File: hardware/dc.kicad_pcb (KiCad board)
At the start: 4 copper layers, 80 x 80 mm, 70 parts, among them P1 CON-SENSOR2, P2 DEBUG, P3 BOOT, P4 OUT, P5 GPIO, P6 IN, Q1 PSMN5R6-60YLX, U1 XMC1???, U2 DRILL, U3 DRILL, U4 DRILL, U5 DRILL, U6 VNH5019A-E, U7 LTV-827

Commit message: new DRV8701 design
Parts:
- C1: footprint C0402E -> kicad-libraries:C0402E
- C4: footprint C0603F -> kicad-libraries:C0603F
- D1, D10, D11, D12, D8, D9: footprint D0603F -> kicad-libraries:D0603F
- P2: footprint DEBUG_PAD -> kicad-libraries:DEBUG_PAD
- P3: footprint SolderJumper -> kicad-libraries:SolderJumper
- P6: footprint kicad-libraries:OQ_2P_5mm_Vertical -> kicad-libraries:OQ_2P_5mm_Vertical_Black
- RP1: footprint 4X0603 -> kicad-libraries:4X0603
- U1: footprint QFN24-4x4mm-0.5mm -> kicad-libraries:QFN24-4x4mm-0.5mm
- U2, U3, U4, U5: footprint DRILL_NP -> kicad-libraries:DRILL_NP

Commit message: new design
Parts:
- removed the Fiducial_Mark at (93.5, 120.5)
- removed the Fiducial_Mark at (88.5, 168.5)
- removed the Fiducial_Mark at (134.5, 118.5)
- removed the G*** at (99.5, 163.5)
- removed PTC1: VC080526C580DP, kicad-libraries:R0805E
- removed RP2: 3,3k, kicad-libraries:4X0603
- removed RP3: 1k, kicad-libraries:0603X4
- removed VAL: CE_5mm, kicad-libraries:CE_5mm
- removed VAL: WEEE_7mm, kicad-libraries:WEEE_7mm
- added C17: DNP, kicad-libraries:C0603F, F.Cu at (124.3, 149.1)
- added C18: 1uF/100V, kicad-libraries:C1206E, F.Cu at (66.0, 131.6)
- added C19: 220uF/100V/UVY2A221MHD1TO, kicad-libraries:ELKO_RAD_12, F.Cu at (66.8, 142.2)
- added C20: DNP, kicad-libraries:C0603F, F.Cu at (94.2, 152.8)
- added C21: DNP, kicad-libraries:C0603F, F.Cu at (111.3, 149.1)
- added C22: 220uF/100V/UVY2A221MHD1TO, kicad-libraries:ELKO_RAD_12, F.Cu at (66.8, 156.0)
- added C23: 1nF/100V, kicad-libraries:C0603F, F.Cu at (122.5, 176.7)
- added C24: 1nF/100V, kicad-libraries:C0603F, F.Cu at (106.5, 176.7)
- added C25: 220uF/100V/UVY2A221MHD1TO, kicad-libraries:ELKO_RAD_12, F.Cu at (79.1, 149.1)
- added C26: 220uF/100V/UVY2A221MHD1TO, kicad-libraries:ELKO_RAD_12, F.Cu at (79.1, 135.1)
- added D13: SMBJ36CA, kicad-libraries:SMB, F.Cu at (74.5, 165.4)
- added Q2: CSD19533Q5A, kicad-libraries:SON_5x6mm, F.Cu at (121.0, 150.9)
- added Q3: CSD19533Q5A, kicad-libraries:SON_5x6mm, F.Cu at (97.5, 151.0)
- added Q4: CSD19533Q5A, kicad-libraries:SON_5x6mm, F.Cu at (108.0, 150.9)
- added Q5: CSD19533Q5A, kicad-libraries:SON_5x6mm, F.Cu at (78.4, 159.8)
- added R18: TBD, kicad-libraries:R0603F, F.Cu at (118.2, 118.8)
- added R19: TBD, kicad-libraries:R0603F, F.Cu at (119.5, 118.8)
- added R20: 0, kicad-libraries:R0603F, F.Cu at (100.8, 152.8)
- added R21: 0, kicad-libraries:R0603F, F.Cu at (104.7, 149.1)
- added R22: 0, kicad-libraries:R0603F, F.Cu at (134.8, 152.8)
- added R23: 0, kicad-libraries:R0603F, F.Cu at (117.7, 149.1)
- added R24: 0,01/WSHM2818R0100FEA, kicad-libraries:R2818, F.Cu at (114.5, 138.2)
- added R25: 100k, kicad-libraries:R0603F, F.Cu at (74.7, 156.3)
- added R26: B72530T6250K062, kicad-libraries:1210, F.Cu at (74.5, 169.7)
- added R5: 100k, kicad-libraries:R0603F, F.Cu at (152.0, 123.1)
- added R6: 10k, kicad-libraries:R0603F, F.Cu at (152.0, 125.4)
- added R7: 1k, kicad-libraries:R0603F, F.Cu at (113.0, 114.7)
- C1: footprint kicad-libraries:C0402E -> C0402E
- C10, C8: value 330uF50V -> 100nF/100V; footprint kicad-libraries:ELKO_103 -> kicad-libraries:C0603F
- C11, C12, C9: value 100nF -> 100nF/100V
- C13: value 1nF/100V -> 10uF/100V; footprint kicad-libraries:C0603F -> kicad-libraries:ELKO_83
- C14: value 1nF/100V -> 1nF
- C15: value 330uF50V -> 1uF/100V; footprint kicad-libraries:ELKO_103 -> kicad-libraries:C1206E
- C16: value 330uF50V -> DNP; footprint kicad-libraries:ELKO_103 -> kicad-libraries:C0603F
- C4: footprint kicad-libraries:C0603F -> C0603F
- C5: value 33nF -> 1uF/16V
- C6, C7: value 1uF/50V -> 1uF/16V; footprint kicad-libraries:C1206E -> kicad-libraries:C0603F
- D1, D10, D11, D12, D8, D9: footprint kicad-libraries:D0603F -> D0603F
- D2: value SDT30B100D1 -> Z12V; footprint kicad-libraries:TO-252-2D -> kicad-libraries:SOD-123
- D3, D4, D5: value SDT30B100D1 -> SMBJ36CA; footprint kicad-libraries:TO-252-2D -> kicad-libraries:SMB
- D6: value ZENER TBD? -> Z3,3V
- D7: value SMBJ24CA -> SMBJ36CA
- P2: footprint kicad-libraries:DEBUG_PAD -> DEBUG_PAD
- P3: footprint kicad-libraries:SolderJumper -> SolderJumper
- Q1: value PSMN5R6-60YLX -> CSD19533Q5A; footprint kicad-libraries:SOT669 -> kicad-libraries:SON_5x6mm
- R2: value 1k -> 7,5k
- R4: value 1k -> 10k
- R8: value 10k -> 1k
- R9: value 1,5k -> 200k
- RP1: footprint kicad-libraries:4X0603 -> 4X0603
- U1: footprint kicad-libraries:QFN24-4x4mm-0.5mm -> QFN24-4x4mm-0.5mm
- U2, U3, U4, U5: footprint kicad-libraries:DRILL_NP -> DRILL_NP
- U6: value VNH5019A-E -> DRV8701; footprint kicad-libraries:VNH5019A-E -> kicad-libraries:QFN24-4x4mm-0.5mm
- moved Q1 66.2 mm to (131.5, 151.0), turned to 270 degrees
- moved C16 61.8 mm to (128.2, 152.8), turned to 270 degrees
- moved C10 56.0 mm to (118.1, 124.6), turned to 270 degrees
- moved C8 50.7 mm to (118.9, 120.9)
- moved R4 36.7 mm to (148.1, 125.4), turned to 0 degrees
- moved R2 35.0 mm to (148.1, 123.1), turned to 0 degrees
- moved C13 35.0 mm to (132.1, 123.7), turned to 180 degrees
- moved D2 34.5 mm to (74.7, 160.5), turned to 90 degrees
- moved D5 30.4 mm to (102.7, 173.4), turned to 0 degrees
- moved D3 30.1 mm to (126.1, 173.4), turned to 180 degrees
- moved D7 29.8 mm to (102.7, 177.7), turned to 180 degrees
- moved G*** 24.6 mm to (45.3, 109.5)
- moved C14 23.0 mm to (113.9, 125.7)
- moved C15 22.0 mm to (66.0, 129.3)
- moved C6 16.4 mm to (116.3, 117.3)
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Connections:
- C10 pad 1: Net-(C10-Pad1) -> V_GPIO
- C13 pad 1: Net-(C13-Pad1) -> V_GPIO
- C15 pad 1: Net-(C10-Pad1) -> V_GPIO
- C16 pad 1: Net-(C10-Pad1) -> V_GPIO
- C16 pad 2: GND -> Net-(C16-Pad2)
- C5 pad 1: CS -> Net-(C5-Pad1)
- C6 pad 1: Net-(C10-Pad1) -> AVDD
- C7 pad 1: Net-(C10-Pad1) -> V_GPIO
- C7 pad 2: GND -> Net-(C7-Pad2)
- C8 pad 1: Net-(C10-Pad1) -> Net-(C8-Pad1)
- C8 pad 2: GND -> Net-(C8-Pad2)
- D2 pad 1: Net-(C13-Pad1) -> GND
- D2 pad 2: Net-(C10-Pad1) -> Net-(D2-Pad2)
- D3 pad 1: GND -> V_GPIO
- D3 pad 2: Net-(C13-Pad1) -> Net-(C16-Pad2)
- D4 pad 1: Net-(C14-Pad1) -> Net-(C16-Pad2)
- D4 pad 2: Net-(C10-Pad1) -> GND
- D5 pad 1: GND -> V_GPIO
- D5 pad 2: Net-(C14-Pad1) -> Net-(C20-Pad2)
- D7 pad 1: V_GPIO -> Net-(C20-Pad2)
- P4 pad 1: Net-(C13-Pad1) -> Net-(C20-Pad2)
- P4 pad 2: Net-(C14-Pad1) -> Net-(C16-Pad2)
- P6 pad 2: GND -> Net-(D13-Pad2)
- Q1 pad D: Net-(C10-Pad1) -> V_GPIO
- Q1 pad S: V_GPIO -> Net-(C16-Pad2)
- R2 pad 2: Enable_Diag_B -> SO
- R4 pad 1: Net-(R4-Pad1) -> GND
- R4 pad 2: IN_B -> Net-(R2-Pad1)
- R8 pad 1: Net-(R8-Pad1) -> +3.3VP
- R8 pad 2: CS -> nFAULT
- R9 pad 1: GND -> Net-(R9-Pad1)
- R9 pad 2: Net-(R8-Pad1) -> GND
- U1 pad 11: Net-(RP5-Pad8) -> Net-(R3-Pad1)
- U1 pad 12: Net-(RP5-Pad7) -> Net-(RP5-Pad8)
- U1 pad 13: Net-(RP5-Pad6) -> Net-(RP5-Pad7)
- U1 pad 14: PWM -> Net-(RP5-Pad6)
- U1 pad 17: IN_B -> IN1
- U1 pad 18: Enable_Diag_B -> IN2
- U1 pad 19: DC_DIS -> nSLEEP
- U1 pad 2: Net-(P2-Pad1) -> GPIO0
- U1 pad 20: Enable_Diag_A -> Net-(P2-Pad1)
- U1 pad 21: IN_A -> Net-(P3-Pad2)
- U1 pad 3: Net-(U1-Pad3) -> SNSOUT
- U1 pad 4: Net-(P3-Pad2) -> nFAULT
- U1 pad 5: GPIO0 -> VIN
- U1 pad 7: Net-(R3-Pad1) -> Net-(U1-Pad7)
- U1 pad 8: CS -> Net-(R2-Pad1)
- U6 pad 1: Net-(C14-Pad1) -> V_GPIO
- U6 pad 10: Net-(R4-Pad1) -> SNSOUT
- U6 pad 11: Net-(Q1-PadG) -> SO
- U6 pad 12: V_GPIO -> Net-(R9-Pad1)
- U6 pad 13: Net-(C10-Pad1) -> nSLEEP
- U6 pad 14: Net-(U6-Pad14) -> IN2
- U6 pad 15: Net-(C13-Pad1) -> IN1
- U6 pad 16: Net-(C13-Pad1) -> GND
- U6 pad 18: GND -> Net-(C20-Pad2)
- U6 pad 19: GND -> Net-(R21-Pad2)
- U6 pad 2: Net-(U6-Pad2) -> Net-(C7-Pad2)
- U6 pad 21: Net-(C13-Pad1) -> Net-(C14-Pad1)
- U6 pad 23: Net-(C10-Pad1) -> Net-(C16-Pad2)
- U6 pad 3: Net-(C10-Pad1) -> Net-(C8-Pad1)
- U6 pad 4: Net-(RP3-Pad8) -> Net-(C8-Pad2)
- U6 pad 5: Net-(RP2-Pad5) -> GND
- U6 pad 7: Net-(RP3-Pad5) -> AVDD
- U6 pad 8: Net-(R8-Pad1) -> Net-(C5-Pad1)
- U6 pad 9: Net-(R2-Pad1) -> nFAULT
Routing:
- net Net-(C11-Pad1): track 86.9 -> 2.87 mm, vias 1 -> 0
- net Net-(C12-Pad1): track 85.4 -> 2.87 mm, vias 1 -> 0
- net Net-(Q1-PadG): track 78.0 -> 0.00 mm, vias 2 -> 0
- net V_GPIO: track 82.8 -> 19.4 mm
- net GPIO0: track 58.1 -> 2.76 mm, vias 2 -> 1
- net GPIO1: track 57.3 -> 2.75 mm, vias 2 -> 1
- net Net-(C10-Pad1): track 31.1 -> 0.00 mm, vias 209 -> 0
- net Net-(RP2-Pad5): track 23.4 -> 0.00 mm, vias 2 -> 0
- net CS: track 19.3 -> 0.00 mm, vias 2 -> 0
- net +3.3VP: track 113.5 -> 94.2 mm
- net Net-(C14-Pad1): track 17.7 -> 0.00 mm, vias 74 -> 1
- net Net-(C13-Pad1): track 17.2 -> 0.00 mm, vias 74 -> 0
- net IN_B: track 16.3 -> 0.00 mm, vias 2 -> 0
- net Enable_Diag_B: track 14.8 -> 0.00 mm, vias 2 -> 0
- net Net-(R2-Pad1): track 13.4 -> 0.00 mm, vias 2 -> 0
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- added copper zone on F.Cu, net Net-(C16-Pad2)
- added copper zone on F.Cu, net Net-(C20-Pad2)
- added copper zone on F.Cu, net Net-(D13-Pad2)
- added copper zone on B.Cu, net V_GPIO
- removed copper zone on B.Cu, net Net-(C1-Pad1)
- removed copper zone on B.Cu, net Net-(C10-Pad1)
- removed copper zone on F.Cu, net Net-(C10-Pad1)
- removed copper zone on B.Cu, net Net-(C13-Pad1)
- removed copper zone on F.Cu, net Net-(C13-Pad1)
- removed copper zone on B.Cu, net Net-(C14-Pad1)
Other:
- board text added: "Input V"

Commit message: new design
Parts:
- removed R7, R8: 1k, kicad-libraries:R0603F
- added RP2: 1k, kicad-libraries:4X0603, F.Cu at (110.1, 116.7)
- moved D7 30.5 mm to (112.4, 148.8), turned to 90 degrees
- moved D4 30.4 mm to (116.6, 148.8), turned to 90 degrees
- moved D5 23.5 mm to (90.8, 153.1), turned to 270 degrees
- moved D3 23.2 mm to (137.4, 153.1), turned to 270 degrees
- moved R6 22.2 mm to (137.4, 108.6)
- moved R4 21.5 mm to (133.8, 109.3), turned to 270 degrees
- moved R5 19.7 mm to (137.4, 109.9), turned to 180 degrees
- moved R2 18.9 mm to (135.1, 109.3), turned to 90 degrees
- moved P2 8.10 mm to (129.8, 117.9)
- moved P3 7.60 mm to (131.6, 117.9), turned to 90 degrees
- moved R9 2.91 mm to (110.1, 119.2), turned to 180 degrees
- moved C4 2.40 mm to (131.3, 109.4)
- moved U1 2.36 mm to (131.3, 113.5)
- moved R10 1.13 mm to (86.7, 112.9), turned to 90 degrees
- moved R11 1.13 mm to (86.7, 116.4), turned to 270 degrees
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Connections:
- U1 pad 17: IN1 -> nSLEEP
- U1 pad 19: nSLEEP -> IN1
- U1 pad 3: SNSOUT -> nFAULT
- U1 pad 4: nFAULT -> SNSOUT
- U1 pad 7: Net-(U1-Pad7) -> Net-(R2-Pad1)
- U1 pad 8: Net-(R2-Pad1) -> Net-(U1-Pad8)
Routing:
- net GPIO1: track 2.75 -> 64.8 mm, vias 1 -> 2
- net GPIO0: track 2.76 -> 58.5 mm, vias 1 -> 0
- net V_GPIO: track 19.4 -> 62.6 mm, vias 2 -> 3
- net Net-(R22-Pad2): track 0.00 -> 37.6 mm, vias 0 -> 2
- net Net-(R20-Pad2): track 0.00 -> 36.0 mm, vias 0 -> 2
- net SO: track 0.00 -> 31.5 mm, vias 0 -> 2
- net Net-(C20-Pad2): track 0.00 -> 31.5 mm, vias 0 -> 2
- net Net-(R21-Pad2): track 0.00 -> 30.8 mm, vias 0 -> 2
- net Net-(C16-Pad2): track 0.00 -> 30.4 mm, vias 0 -> 2
- net SNSOUT: track 0.00 -> 30.3 mm, vias 0 -> 2
- net nFAULT: track 0.00 -> 30.1 mm, vias 0 -> 2
- net Net-(R23-Pad2): track 0.00 -> 28.0 mm, vias 0 -> 2
- net IN1: track 0.00 -> 23.8 mm, vias 0 -> 2
- net IN2: track 0.00 -> 23.3 mm, vias 0 -> 2
- net nSLEEP: track 0.00 -> 22.9 mm, vias 0 -> 2
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
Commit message: safety save
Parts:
- moved D4 39.1 mm to (118.2, 187.9)
- moved D7 39.1 mm to (114.0, 187.9)
- moved D5 38.8 mm to (107.8, 188.0)
- moved D3 36.9 mm to (125.0, 187.9)
- moved R25 5.20 mm to (74.8, 161.5), turned to 90 degrees
- moved D2 3.20 mm to (74.8, 157.3), turned to 270 degrees
- moved C26 1.92 mm to (78.2, 133.4)
- moved C25 1.75 mm to (78.2, 147.6)
- moved C19 1.75 mm to (66.4, 140.5)
- moved C22 1.46 mm to (66.4, 154.6)
- moved C18 0.40 mm to (66.0, 132.0)
- moved C15 0.40 mm to (66.0, 129.7)
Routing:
- net Net-(R22-Pad2): track 37.6 -> 46.4 mm
- net GND: track 30.9 -> 36.6 mm, vias 25 -> 264
- net Net-(D2-Pad2): track 0.00 -> 4.88 mm
- net Net-(C16-Pad2): track 30.4 -> 34.2 mm
- net Net-(R21-Pad2): track 30.8 -> 33.9 mm
- net V_GPIO: track 62.6 -> 65.3 mm, vias 3 -> 149
- net Net-(R20-Pad2): track 36.0 -> 37.8 mm
- net Net-(Q1-PadG): track 0.00 -> 1.46 mm
- net Net-(Q4-PadG): track 0.00 -> 1.46 mm
- net Net-(Q2-PadG): track 0.00 -> 1.46 mm
- net Net-(Q3-PadG): track 0.00 -> 1.46 mm
- net Net-(C20-Pad2): track 31.5 -> 32.5 mm

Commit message: ready for prototype
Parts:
- moved G*** 55.3 mm to (99.5, 120.5)
- moved D7 26.7 mm to (93.3, 171.1), turned to 180 degrees
- moved D5 25.8 mm to (93.3, 166.7), turned to 0 degrees
- moved D4 24.3 mm to (135.7, 171.1), turned to 0 degrees
- moved D3 23.7 mm to (135.7, 166.7), turned to 180 degrees
- moved C23 6.58 mm to (129.0, 177.7)
- moved C24 6.58 mm to (100.0, 177.7)
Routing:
- net Net-(C11-Pad1): track 2.87 -> 90.4 mm, vias 0 -> 1
- net Net-(C12-Pad1): track 2.87 -> 87.4 mm, vias 0 -> 1
- net GND: track 36.6 -> 49.9 mm, vias 264 -> 211
- net Net-(C16-Pad2): track 34.2 -> 45.8 mm
- net Net-(C20-Pad2): track 32.5 -> 44.1 mm
- net V_GPIO: vias 149 -> 252
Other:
- board text removed: "Input 5,5-24V"

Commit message: added input voltage to silkscreen and drc
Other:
- board text added: "Input 6-45V"
- board text removed: "Input V"
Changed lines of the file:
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@@
     (pcbplotparams
       (layerselection 0x010fc_ffffffff)
-      (usegerberextensions false)
+      (usegerberextensions true)
       (usegerberattributes false)
       (usegerberadvancedattributes false)
@@
       (drillshape 0)
       (scaleselection 1)
-      (outputdirectory "../../../DC/"))
+      (outputdirectory "../../../Schreibtisch/proto/dc/"))
   )
   (net 0 "")
@@
     (effects (font (size 2 2) (thickness 0.25)) (justify mirror))
   )
-  (gr_text "Input\nV" (at 74.5 170.7) (layer B.SilkS)
+  (gr_text "Input\n6-45V" (at 74.5 170.7) (layer B.SilkS)
     (effects (font (size 1 1) (thickness 0.15)) (justify mirror))
   )
@@
     (effects (font (size 2 2) (thickness 0.25)))
   )
-  (gr_text "Input\nV" (at 64.6 172.7) (layer F.SilkS)
+  (gr_text "Input\n6-45V" (at 65.05 172.3) (layer F.SilkS)
     (effects (font (size 1 1) (thickness 0.15)))
   )
@@
   (gr_line (start 139.5 103) (end 139.5 178) (layer Edge.Cuts) (width 0.05))
   (gr_line (start 62 100.5) (end 137 100.5) (layer Edge.Cuts) (width 0.05))
+  (segment (start 103.5009 107.5491) (end 103.5 107.55) (width 0.2) (layer F.Cu) (net 1))
+  (segment (start 103.25 107.3) (end 103.5 107.55) (width 0.2) (layer F.Cu) (net 1))
+  (segment (start 103.25 105.4) (end 103.25 107.3) (width 0.2) (layer F.Cu) (net 1))
+  (segment (start 102.49798 107.55) (end 102.39888 107.6491) (width 0.2) (layer F.Cu) (net 1))
+  (segment (start 103.5 107.55) (end 102.49798 107.55) (width 0.2) (layer F.Cu) (net 1))
   (via (at 136.6 169.5) (size 0.5) (drill 0.2) (layers F.Cu B.Cu) (net 2))
   (via (at 89.75 169.55) (size 0.5) (drill 0.2) (layers F.Cu B.Cu) (net 2))
@@
   (via (at 136.7 125.2) (size 0.8) (drill 0.4) (layers F.Cu B.Cu) (net 2))
   (via (at 134.9 125.2) (size 0.8) (drill 0.4) (layers F.Cu B.Cu) (net 2))
-  (segment (start 103.5009 107.5491) (end 103.5 107.55) (width 0.2) (layer F.Cu) (net 1))
-  (segment (start 103.25 107.3) (end 103.5 107.55) (width 0.2) (layer F.Cu) (net 1))
-  (segment (start 103.25 105.4) (end 103.25 107.3) (width 0.2) (layer F.Cu) (net 1))
-  (segment (start 102.49798 107.55) (end 102.39888 107.6491) (width 0.2) (layer F.Cu) (net 1))
-  (segment (start 103.5 107.55) (end 102.49798 107.55) (width 0.2) (layer F.Cu) (net 1))
   (via (at 115.4 120.8) (size 0.5) (drill 0.2) (layers F.Cu B.Cu) (net 2))
   (via (at 113.6 122.6) (size 0.5) (drill 0.2) (layers F.Cu B.Cu) (net 2))

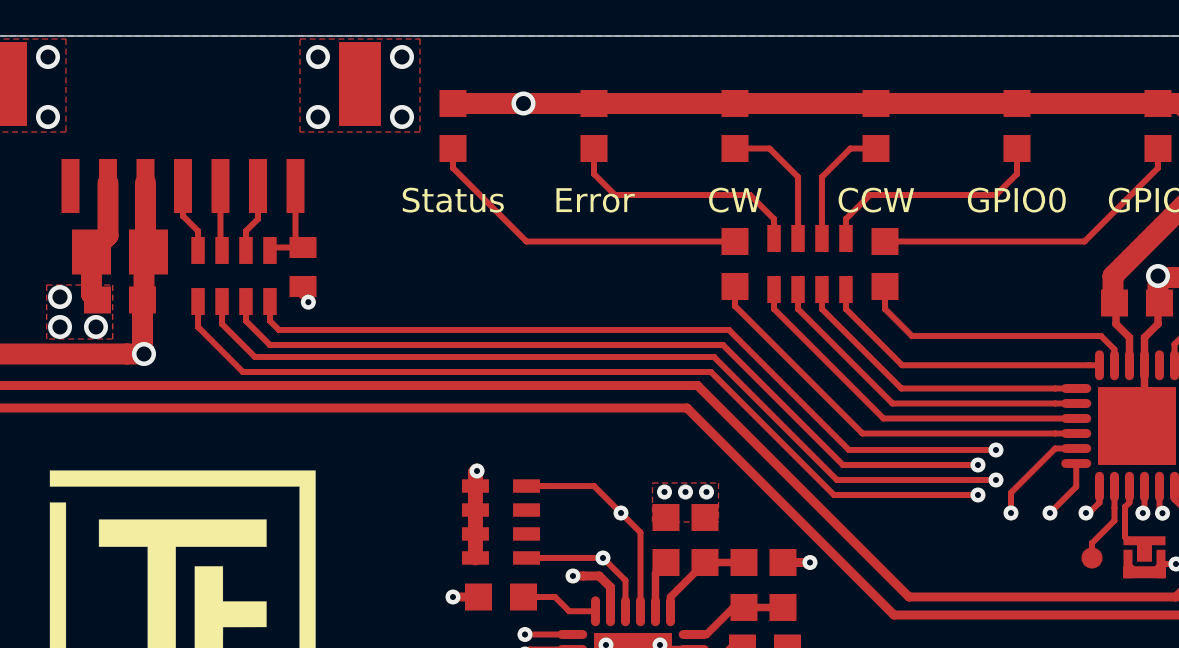
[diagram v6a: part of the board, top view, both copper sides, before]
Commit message: changed resistor footprint
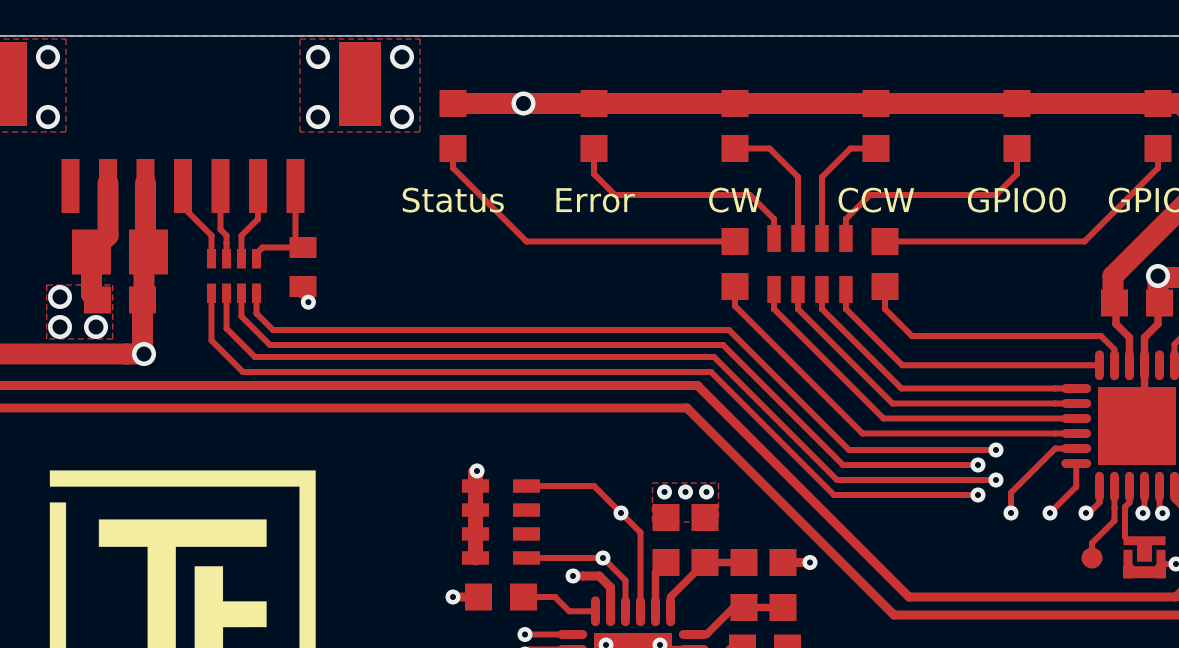
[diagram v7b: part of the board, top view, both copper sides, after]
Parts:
- RP1: footprint 4X0603 -> tinkerforge:4X0402
- turned RP1 to 180 degrees
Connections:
- RP1 pad 1: Net-(P1-Pad4) -> Net-(C1-Pad1)
- RP1 pad 2: Net-(P1-Pad5) -> Net-(P1-Pad6)
- RP1 pad 3: Net-(P1-Pad6) -> Net-(P1-Pad5)
- RP1 pad 4: Net-(C1-Pad1) -> Net-(P1-Pad4)
- RP1 pad 5: S-MISO -> S-CS
- RP1 pad 6: S-MOSI -> S-CLK
- RP1 pad 7: S-CLK -> S-MOSI
- RP1 pad 8: S-CS -> S-MISO
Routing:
- net Net-(C1-Pad1): track 3.40 -> 4.06 mm

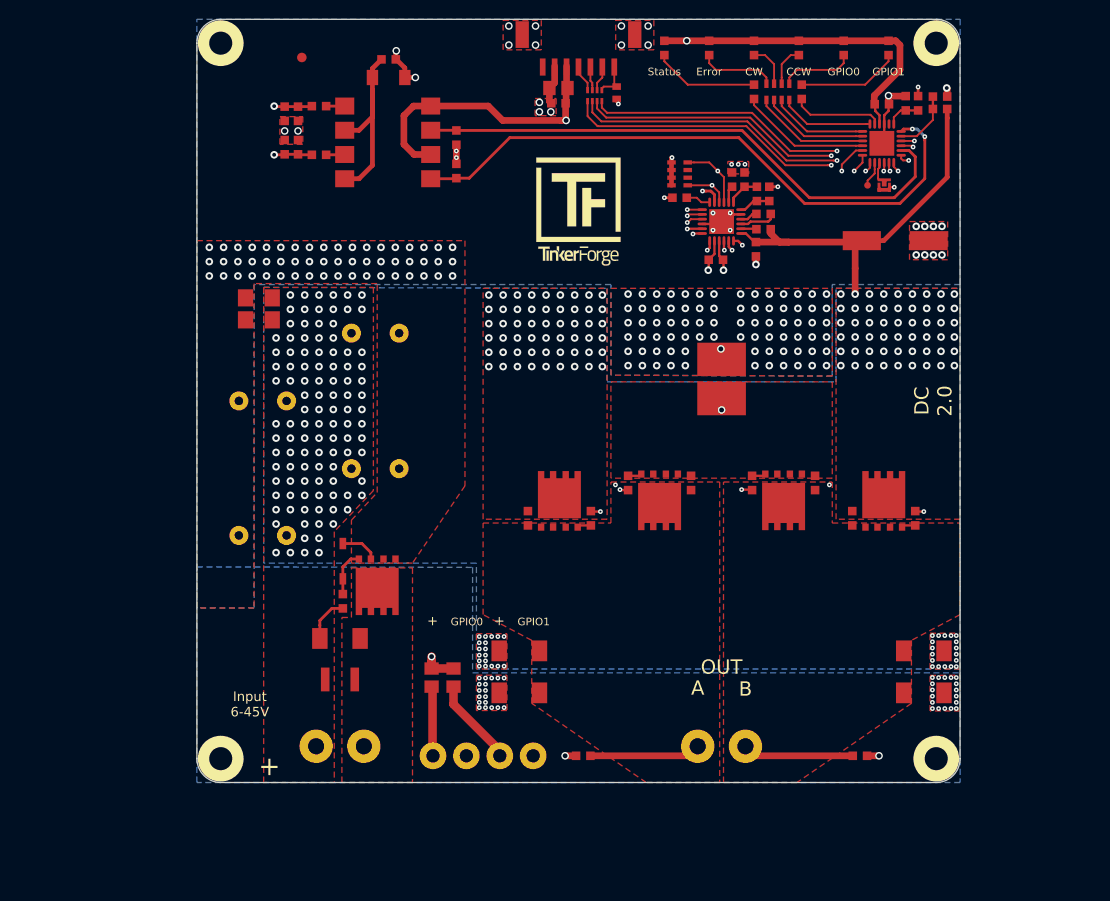
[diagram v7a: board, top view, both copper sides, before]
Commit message: added temperature sensor, and changed protection diodes
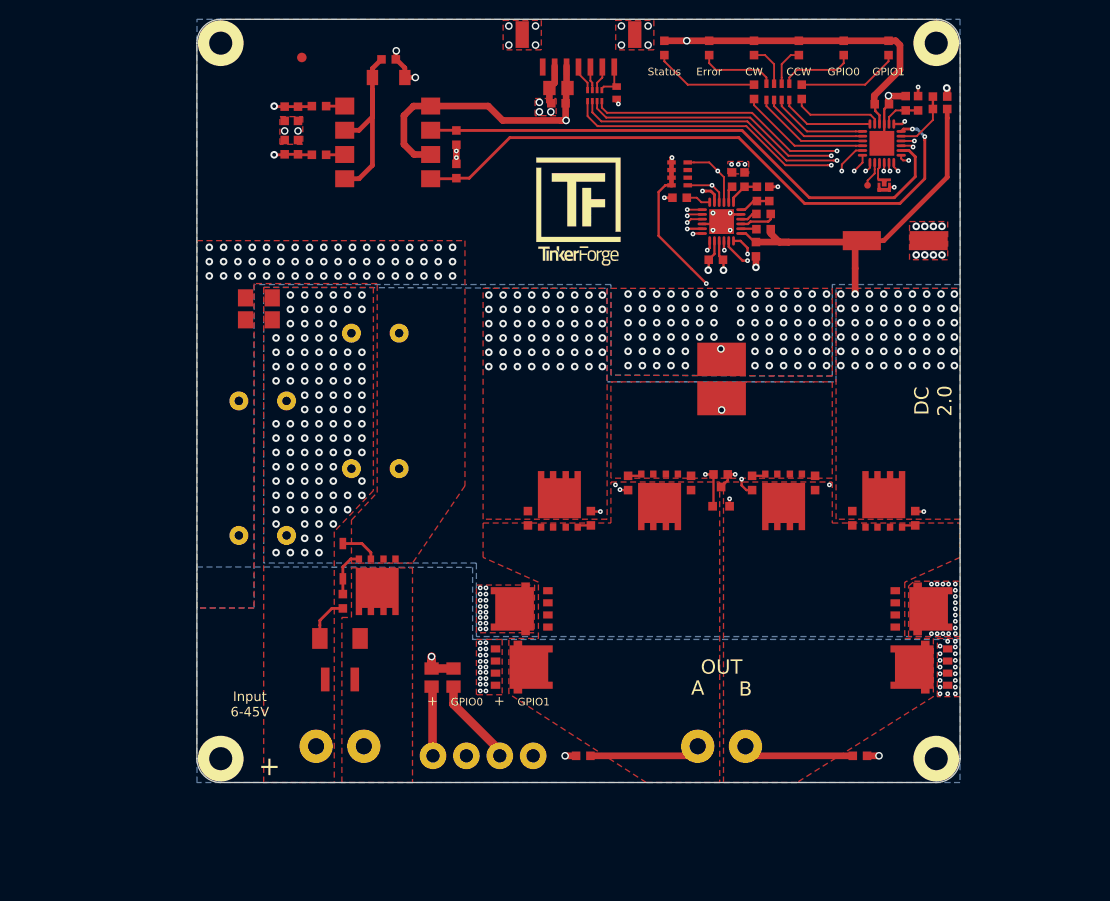
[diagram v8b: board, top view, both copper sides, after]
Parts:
- added C27: 100nF, kicad-libraries:C0603F, F.Cu at (114.4, 148.2)
- added U8: TMP235, kicad-libraries:SOT23-3, F.Cu at (114.4, 150.5)
- D3, D4, D5, D7: value SMBJ36CA -> NTS12120EMFST1G; footprint kicad-libraries:SMB -> kicad-libraries:DFN5_5x6
- moved D5 4.40 mm to (93.5, 162.3), turned to 270 degrees
- moved D3 4.40 mm to (135.5, 162.3), turned to 90 degrees
- moved D7 2.72 mm to (93.6, 168.4), turned to 90 degrees
- moved D4 2.72 mm to (135.4, 168.4), turned to 270 degrees
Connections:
- D3 pad 1: V_GPIO -> Net-(C16-Pad2)
- D3 pad 2: Net-(C16-Pad2) -> V_GPIO
- D4 pad 1: Net-(C16-Pad2) -> GND
- D4 pad 2: GND -> Net-(C16-Pad2)
- D5 pad 1: V_GPIO -> Net-(C20-Pad2)
- D5 pad 2: Net-(C20-Pad2) -> V_GPIO
- D7 pad 1: Net-(C20-Pad2) -> GND
- D7 pad 2: GND -> Net-(C20-Pad2)
- U1 pad 7: Net-(R2-Pad1) -> TEMP
- U1 pad 8: Net-(U1-Pad8) -> Net-(R2-Pad1)
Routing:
- net TEMP: track 0.00 -> 60.0 mm, vias 0 -> 2
- net +3.3VP: track 92.4 -> 130.0 mm, vias 3 -> 5
- net GND: track 49.9 -> 67.9 mm, vias 211 -> 213
- net V_GPIO: track 65.3 -> 71.3 mm, vias 252 -> 249
- net Net-(R2-Pad1): track 3.62 -> 4.14 mm
